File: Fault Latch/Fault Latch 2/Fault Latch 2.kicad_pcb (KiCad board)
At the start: 2 copper layers, 110 x 90 mm, 108 parts, among them K101 Fujitsu_FTR-LYAA005x, K102 Fujitsu_FTR-LYAA005x, K103 Fujitsu_FTR-LYAA005x, Q101 Q_NPN_BEC, Q102 Q_NPN_BEC, Q103 Q_NPN_BEC, Q104 Q_NPN_BEC, Q105 Q_NMOS_GSD, Q106 Q_NMOS_GSD, Q107 Q_PMOS_GSD, Q108 Q_PMOS_GSD, Q109 Q_NMOS_GDS, Q110 Q_NPN_BEC, Q111 Q_NPN_BEC, Q112 Q_NMOS_GSD, Q113 Q_PMOS_GSD, SW101 SW_Omron_B3FS, SW102 SW_Omron_B3FS, SW103 SW_Omron_B3FS, U101 SFH617A-1, U102 SFH617A-1, U103 SFH617A-1, U104 74AHC1G00, U105 74AHC1G00, U106 74AHC1G00, U107 74LS279, U108 641964-1, U109 SFH617A-1, U110 SFH617A-1, U111 641964-1, U112 641964-1, U113 641964-1, U114 641964-1, U115 641964-1, U116 641964-1, U117 74AHC1G00, U118 LM555xM, U119 74AHC1G00, U120 641964-1, U121 SFH617A-1, U122 641964-1

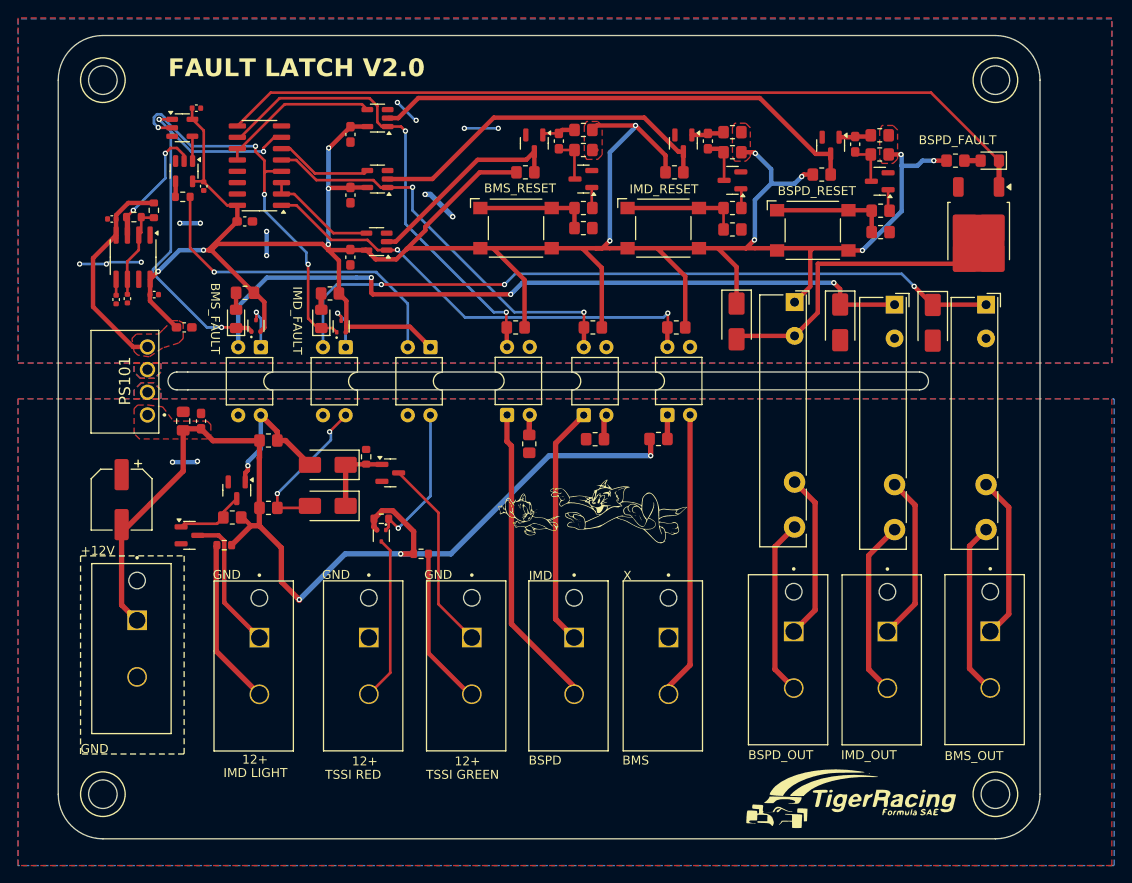
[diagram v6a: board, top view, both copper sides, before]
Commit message: Rerouted for grounding
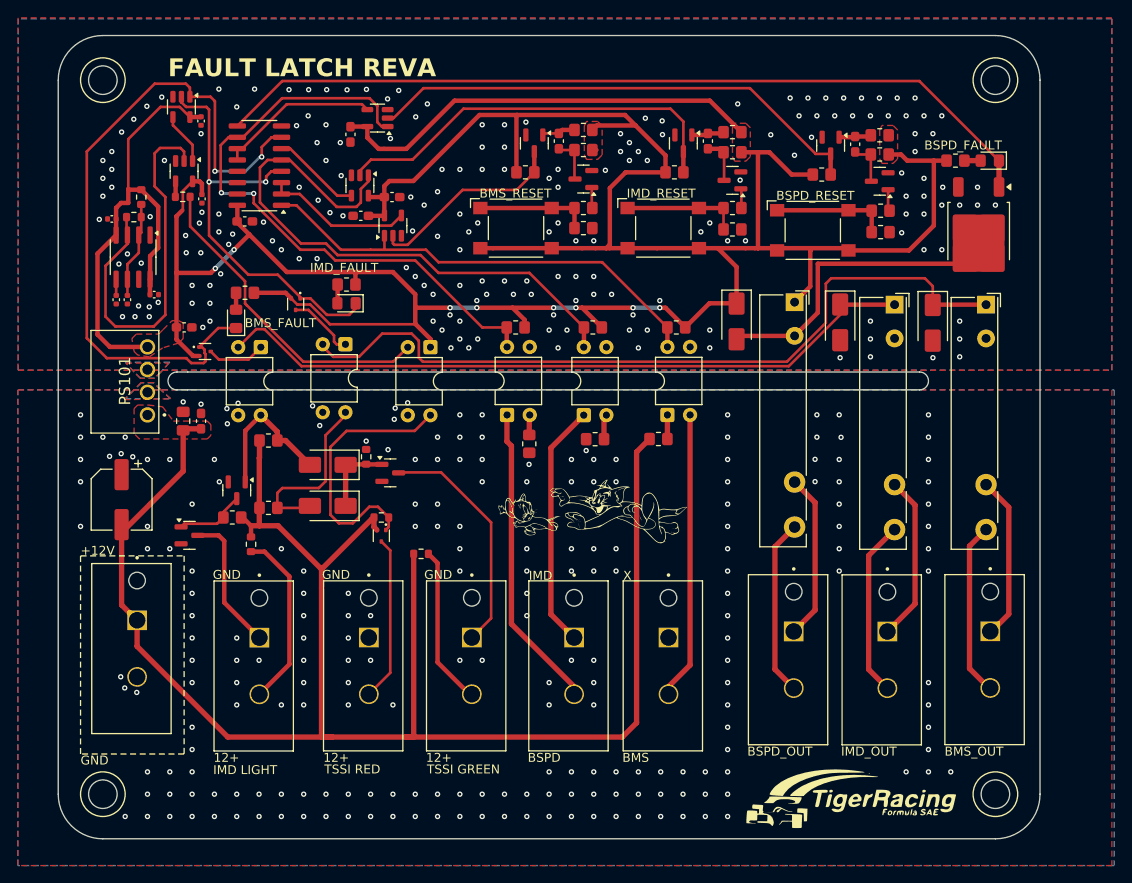
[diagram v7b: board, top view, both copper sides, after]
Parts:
- moved Q108 6.39 mm to (85.7, 79.5), turned to 0 degrees
- moved Q107 5.68 mm to (95.8, 74.2), turned to -90 degrees
- moved C104 4.79 mm to (103.1, 64.3), turned to 180 degrees
- moved C102 4.66 mm to (106.6, 62.2), turned to 0 degrees
- moved D102 3.32 mm to (101.5, 74.1), turned to 180 degrees
- moved R112 3.00 mm to (90.8, 101.1), turned to -90 degrees
- moved U104 2.57 mm to (106.7, 65.4), turned to 90 degrees
- moved U117 2.34 mm to (83.0, 52.1), turned to -90 degrees
- moved R117 2.10 mm to (101.5, 72.0)
- moved U105 2.09 mm to (103.0, 60.9), turned to -90 degrees
- moved R132 2.05 mm to (78.5, 62.2)
- moved C110 1.53 mm to (85.2, 53.7), turned to 90 degrees
- moved C112 1.43 mm to (85.3, 62.4)
- moved U109 0.33 mm to (101.4, 78.7)
- moved R134 0.14 mm to (105.4, 98.1)
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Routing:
- net +5V: track 317.5 -> 407.3 mm, vias 13 -> 8
- net +12V: track 118.6 -> 196.6 mm, vias 3 -> 0
- net /IMD_SR: track 48.2 -> 79.1 mm, vias 3 -> 2
- net /CLOCK: track 14.3 -> 43.4 mm, vias 2 -> 0
- net GND: track 22.9 -> 0.00 mm, vias 13 -> 192
- net /NIMD_LV: track 46.4 -> 65.6 mm, vias 2 -> 0
- net /NBPSD_LV: track 53.0 -> 69.7 mm
- net Net-(Q113-G): track 17.1 -> 29.9 mm, vias 1 -> 0
- net /NRESET_IMD: track 39.9 -> 45.9 mm
- net Net-(D104-K): track 82.4 -> 87.5 mm, vias 3 -> 0
- net Net-(Q112-D): track 21.8 -> 26.5 mm
- net /BMS_SR: track 43.8 -> 48.2 mm, vias 4 -> 2
- net Net-(D106-K): track 83.8 -> 79.7 mm, vias 3 -> 0
- net Net-(U104-Pad4): track 12.6 -> 16.6 mm
- net Net-(U117-Pad4): track 2.78 -> 5.85 mm
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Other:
- board text added: "FAULT LATCH REVA"
- board text removed: "FAULT LATCH V2.0"

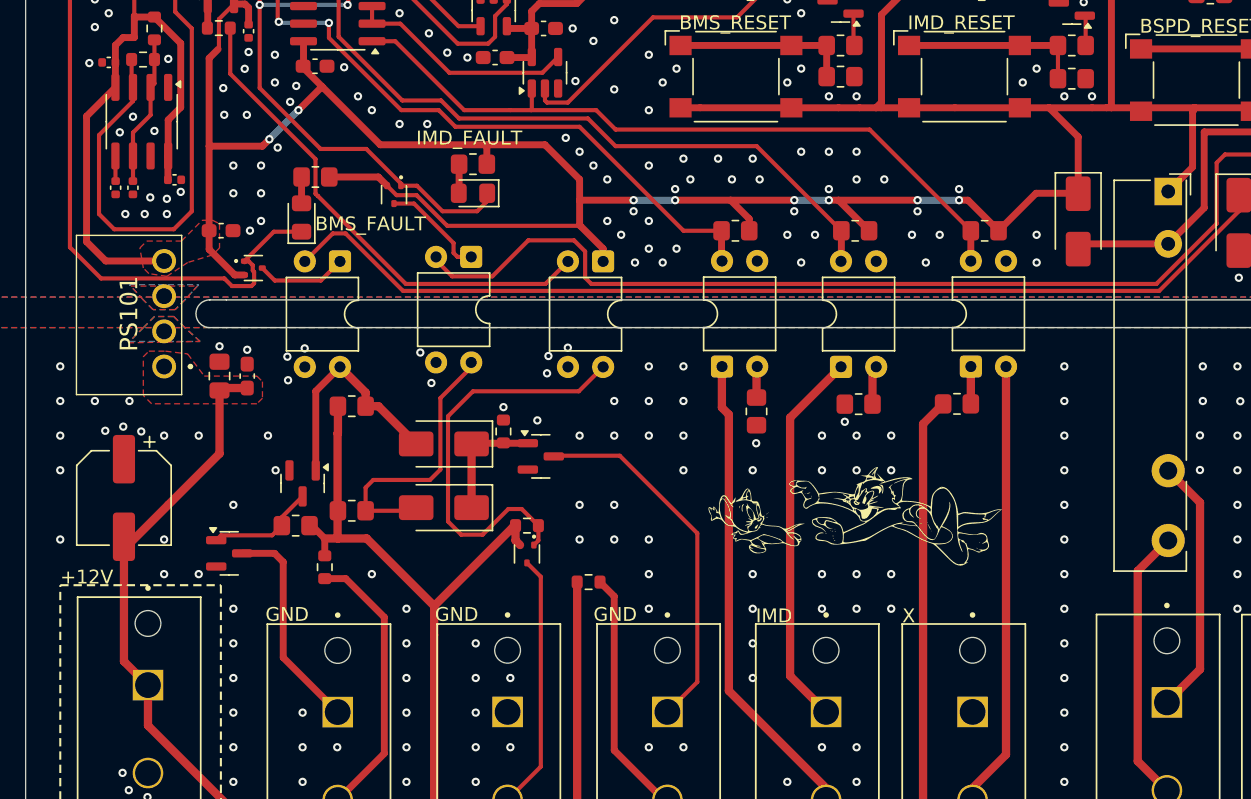
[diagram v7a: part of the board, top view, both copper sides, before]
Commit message: Fault Latch Updated and generated gerber files
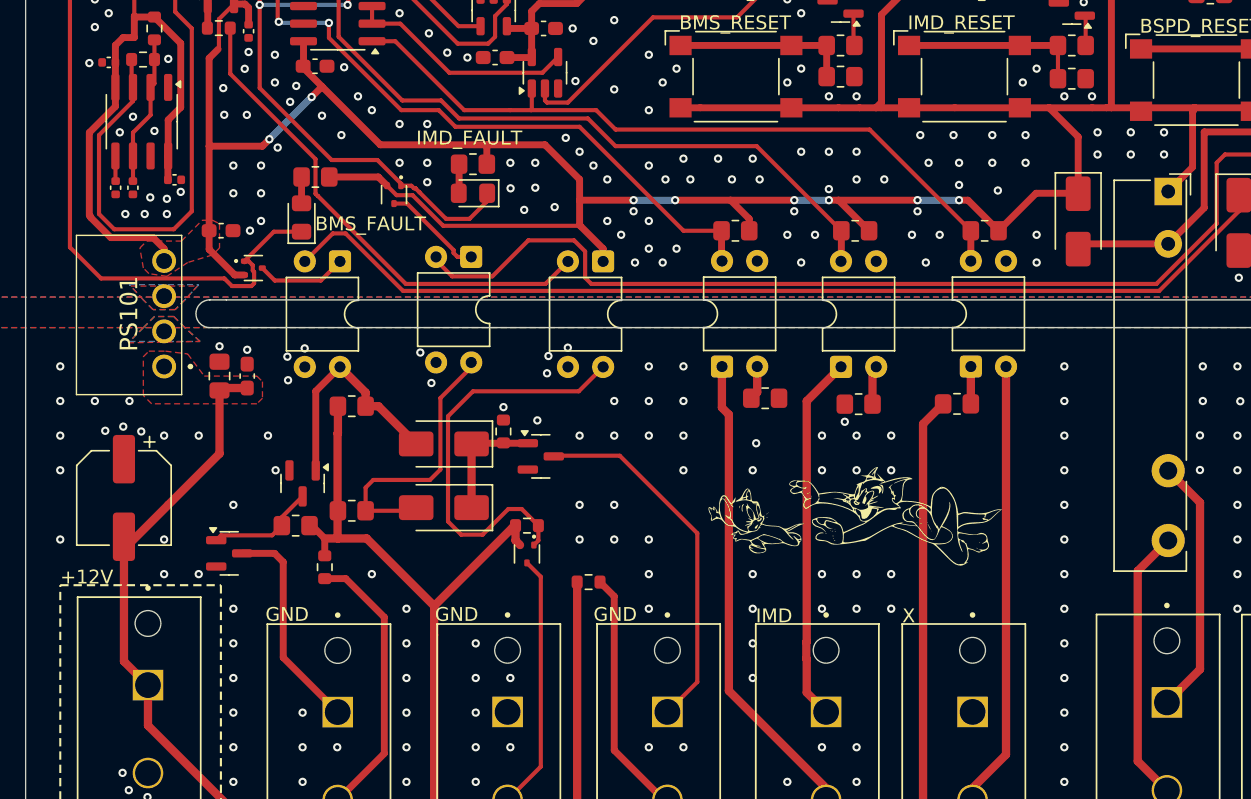
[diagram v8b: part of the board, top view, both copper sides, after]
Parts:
- moved R104 1.14 mm to (122.6, 88.9), turned to 180 degrees
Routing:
- net /IMD_HV: track 27.5 -> 26.5 mm
- net +5V: track 407.3 -> 406.5 mm
- net GND: vias 192 -> 218
